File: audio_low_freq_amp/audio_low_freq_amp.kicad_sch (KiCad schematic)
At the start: 11 parts, among them Q1 NPN, Q2 PNP

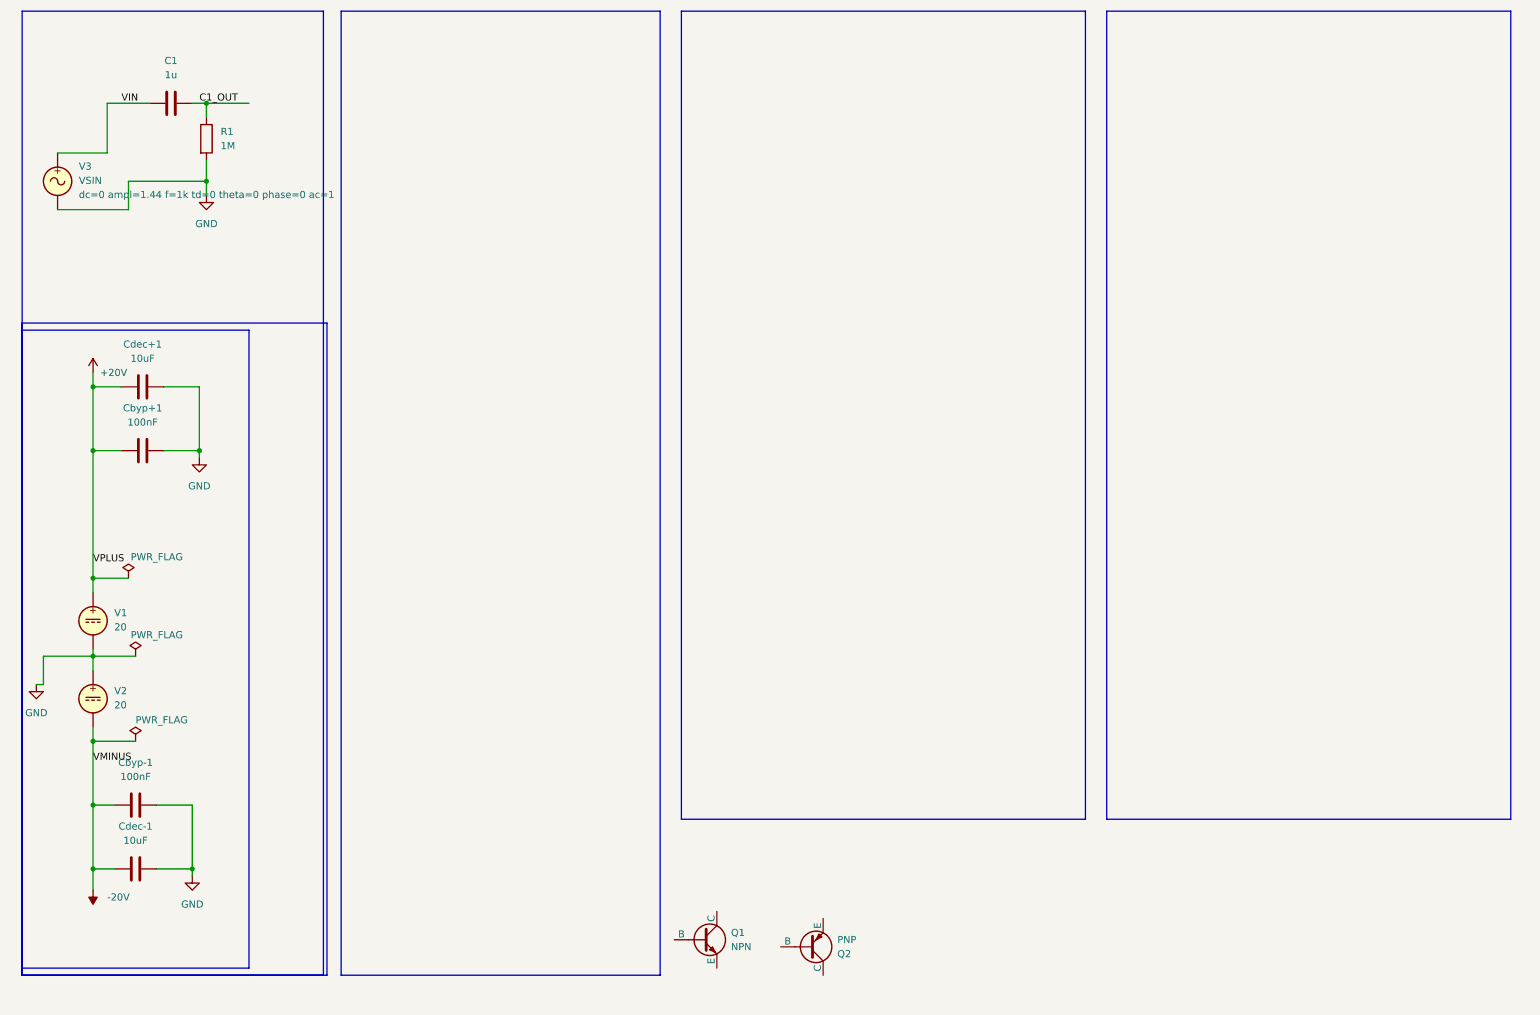
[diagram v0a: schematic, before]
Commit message: finished unrefined version of the schematic with a new approach in mind. works very good for beginning, but needs more work. great place to start bc we almost got a sine wave at output and gain is a little to big, but in normal range of error. note that at 20kHz it starts to distort a little bit
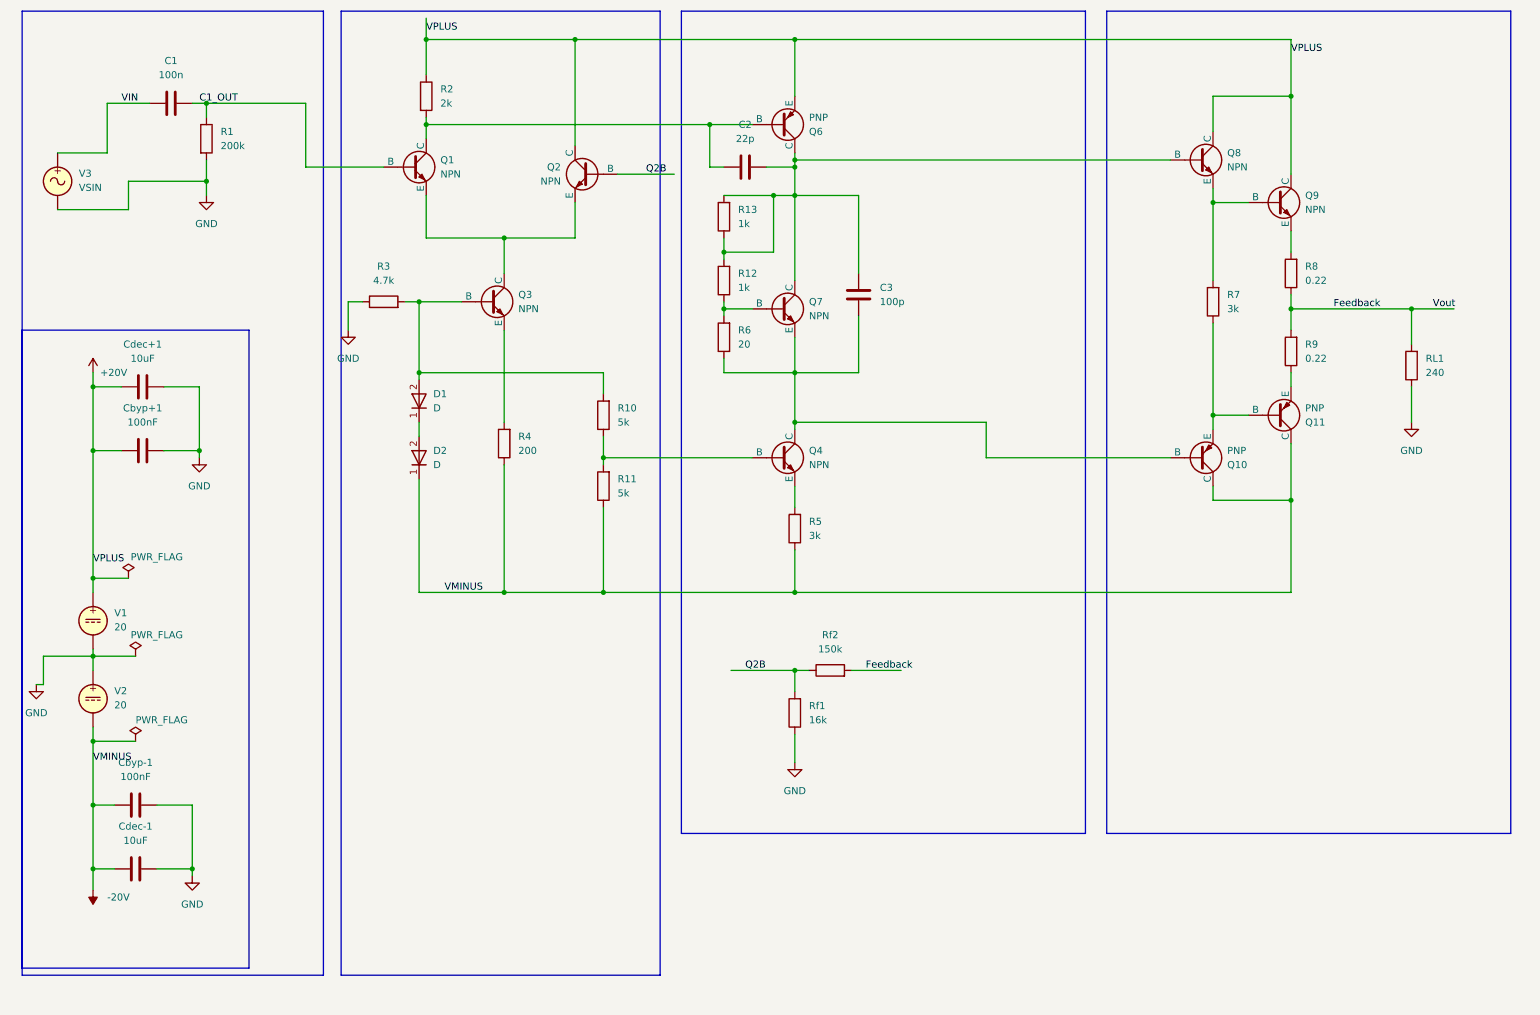
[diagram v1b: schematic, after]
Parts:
- removed Q2: PNP, symbol Simulation_SPICE:PNP
- added C2: 22p, symbol Device:C
- added C3: 100p, symbol Device:C
- added D1, D2: D, symbol Simulation_SPICE:D
- added Q10, Q11, Q6: PNP, symbol Simulation_SPICE:PNP
- added Q2, Q3, Q4, Q7, Q8, Q9: NPN, symbol Simulation_SPICE:NPN
- added R10, R11: 5k, symbol Device:R
- added R12, R13: 1k, symbol Device:R
- added R2: 2k, symbol Device:R
- added R3: 4.7k, symbol Device:R
- added R4: 200, symbol Device:R
- added R5, R7: 3k, symbol Device:R
- added R6: 20, symbol Device:R
- added R8, R9: 0.22, symbol Device:R
- added RL1: 240, symbol Device:R
- added Rf1: 16k, symbol Device:R
- added Rf2: 150k, symbol Device:R
- C1: value 1u -> 100n
- R1: value 1M -> 200k
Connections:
- net +20V: now also Q2.1 (C), Q6.3 (E), Q8.1 (C), Q9.1 (C), R2.1
- net -20V: now also D2.1 (K), Q10.1 (C), Q11.1 (C), R11.1, R4.1, R5.1
- net C1_OUT: now also Q1.2 (B)
- net GND: now also R3.1, RL1.1, Rf1.1
- net at Q1.1 (C): now also C2.1, Q6.2 (B), R2.2
- net at Q1.3 (E): now also Q2.3 (E), Q3.1 (C)
- new net: C3.1, Q10.2 (B), Q4.1 (C), Q7.3 (E), R6.1
- new net: C2.2, C3.2, Q6.1 (C), Q7.1 (C), Q8.2 (B), R12.2, R13.1, R13.2
- new net: Q4.3 (E), R5.2
- new net: Q3.3 (E), R4.2
- new net: Q10.3 (E), Q11.2 (B), R7.1
- new net: Q11.3 (E), R9.1
- new net: Q8.3 (E), Q9.2 (B), R7.2
- new net: D1.2 (A), Q3.2 (B), R10.2, R3.2
- new net: Q4.2 (B), R10.1, R11.2
- new net: D1.1 (K), D2.2 (A)
- new net: Q7.2 (B), R12.1, R6.2
- new net: Q9.3 (E), R8.2
- new net Feedback: R8.1, R9.2, RL1.2, Rf2.2
- new net Q2B: Q2.2 (B), Rf1.2, Rf2.1
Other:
- moved on the sheet: Q1

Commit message: commit before going to check up with the professor
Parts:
- removed R13: 1k, symbol Device:R
- C1: value 100n -> 100u
- C3: value 100p -> 100u
- R10: value 5k -> 3k
- R11: value 5k -> 6k
- R12: value 1k -> 2k
- R6: value 20 -> 1k
- R7: value 3k -> 5k
- Rf1: value 16k -> 10k
- Rf2: value 150k -> 90k
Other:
- moved on the sheet: R12
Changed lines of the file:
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@@
 	)
 	(junction
-		(at 148.59 52.07)
-		(diameter 0)
-		(color 0 0 0 0)
-	)
-	(junction
-		(at 139.7 62.23)
-		(diameter 0)
-		(color 0 0 0 0)
-	)
-	(junction
 		(at 152.4 123.19)
 		(diameter 0)
@@
 	(wire
 		(pts
-			(xy 139.7 71.12) (xy 139.7 72.39)
+			(xy 139.7 66.04) (xy 139.7 72.39)
 		)
 		(stroke
@@
 	(wire
 		(pts
-			(xy 139.7 62.23) (xy 139.7 59.69)
+			(xy 139.7 52.07) (xy 139.7 58.42)
 		)
 		(stroke
@@
 	(wire
 		(pts
-			(xy 139.7 62.23) (xy 148.59 62.23)
-		)
-		(stroke
-			(width 0)
-			(type default)
-		)
-	)
-	(wire
-		(pts
 			(xy 139.7 73.66) (xy 139.7 72.39)
 		)
@@
 	(wire
 		(pts
-			(xy 148.59 52.07) (xy 152.4 52.07)
-		)
-		(stroke
-			(width 0)
-			(type default)
-		)
-	)
-	(wire
-		(pts
 			(xy 262.89 72.39) (xy 262.89 78.74)
 		)
@@
 	(wire
 		(pts
-			(xy 148.59 52.07) (xy 148.59 62.23)
-		)
-		(stroke
-			(width 0)
-			(type default)
-		)
-	)
-	(wire
-		(pts
 			(xy 17.78 134.62) (xy 26.67 134.62)
 		)
@@
 	(wire
 		(pts
-			(xy 139.7 52.07) (xy 148.59 52.07)
+			(xy 139.7 52.07) (xy 152.4 52.07)
 		)
 		(stroke
@@
 	(wire
 		(pts
-			(xy 139.7 62.23) (xy 139.7 63.5)
-		)
-		(stroke
-			(width 0)
-			(type default)
-		)
-	)
-	(wire
-		(pts
 			(xy 26.67 133.35) (xy 26.67 134.62)
 		)
@@
 			)
 		)
-		(property "Value" "100n"
+		(property "Value" "100u"
 			(at 40.64 30.48 90)
 			(effects
@@
 			)
 		)
-		(property "Value" "100p"
+		(property "Value" "100u"
 			(at 167.64 71.1199 0)
 			(effects
@@
 			)
 		)
-		(property "Sim.Params" "dc=0 ampl=1.44 f=20k td=0 theta=0 phase=0 ac=1"
+		(property "Sim.Params" "dc=0 ampl=1.44 f=10k td=0 theta=0 phase=0 ac=1"
 			(at 24.13 51.9401 0)
 			(effects
@@
 	)
 	(symbol
-		(lib_id "Device:R")
-		(at 139.7 55.88 180)
-		(unit 1)
-		(exclude_from_sim no)
-		(in_bom yes)
-		(on_board yes)
-		(dnp no)
-		(fields_autoplaced yes)
-		(property "Reference" "R13"
-			(at 142.24 54.6099 0)
-			(effects
-				(font
-					(size 1.27 1.27)
-				)
-				(justify right)
-			)
-		)
-		(property "Value" "1k"
-			(at 142.24 57.1499 0)
-			(effects
-				(font
-					(size 1.27 1.27)
-				)
-				(justify right)
-			)
-		)
-		(property "Footprint" ""
-			(at 141.478 55.88 90)
-			(effects
-				(font
-					(size 1.27 1.27)
-				)
-				(hide yes)
-			)
-		)
-		(property "Datasheet" "~"
-			(at 139.7 55.88 0)
-			(effects
-				(font
-					(size 1.27 1.27)
-				)
-				(hide yes)
-			)
-		)
-		(property "Description" "Resistor"
-			(at 139.7 55.88 0)
-			(effects
-				(font
-					(size 1.27 1.27)
-				)
-				(hide yes)
-			)
-		)
-		(pin "2"
-		)
-		(pin "1"
-		)
-		(instances
-			(project "audio_low_freq_amp"
-				(path "/81945fdf-1028-429c-9d81-15fb539a69d7"
-					(reference "R13")
-					(unit 1)
-				)
-			)
-		)
-	)
-	(symbol
 		(lib_id "Simulation_SPICE:PNP")
 		(at 238.76 91.44 0)
@@
 			)
 		)
-		(property "Value" "5k"
+		(property "Value" "3k"
 			(at 120.65 92.7099 0)
 			(effects
@@
 	(symbol
 		(lib_id "Device:R")
-		(at 139.7 67.31 180)
+		(at 139.7 62.23 180)
 		(unit 1)
 		(exclude_from_sim no)
@@
 		(fields_autoplaced yes)
 		(property "Reference" "R12"
-			(at 142.24 66.0399 0)
+			(at 142.24 60.9599 0)
 			(effects
 				(font
@@
 			)
 		)
-		(property "Value" "1k"
-			(at 142.24 68.5799 0)
+		(property "Value" "2k"
+			(at 142.24 63.4999 0)
 			(effects
 				(font
@@
 		)
 		(property "Footprint" ""
-			(at 141.478 67.31 90)
+			(at 141.478 62.23 90)
 			(effects
 				(font
@@
 		)
 		(property "Datasheet" "~"
-			(at 139.7 67.31 0)
+			(at 139.7 62.23 0)
 			(effects
 				(font
@@
 		)
 		(property "Description" "Resistor"
-			(at 139.7 67.31 0)
+			(at 139.7 62.23 0)
 			(effects
 				(font
@@
 			)
 		)
-		(property "Value" "5k"
+		(property "Value" "6k"
 			(at 120.65 105.4099 0)
 			(effects
@@
 			)
 		)
-		(property "Value" "16k"
+		(property "Value" "10k"
 			(at 154.94 146.0499 0)
 			(effects
@@
 			)
 		)
-		(property "Value" "3k"
+		(property "Value" "5k"
 			(at 229.87 72.3899 0)
 			(effects
@@
 			)
 		)
-		(property "Value" "20"
+		(property "Value" "1k"
 			(at 142.24 78.7399 0)
 			(effects
@@
 			)
 		)
-		(property "Value" "150k"
+		(property "Value" "90k"
 			(at 158.75 133.35 90)
 			(effects

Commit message: modified final sch in tina and kicad
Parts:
- removed Q1, Q2: NPN, symbol Simulation_SPICE:NPN
- removed Q10, Q6: PNP, symbol Simulation_SPICE:PNP
- removed R11: 6k, symbol Device:R
- removed Rf1: 10k, symbol Device:R
- removed Rf2: 90k, symbol Device:R
- added C4: 10u, symbol Device:C
- added D3, D4: LED, LED_SMD:LED_0805_2012Metric, symbol Device:LED
- added Q1, Q11, Q2, Q5, Q8: PNP, symbol Simulation_SPICE:PNP
- added Q12, Q6: NPN, symbol Simulation_SPICE:NPN
- added R13: 2.7k, Resistor_SMD:R_0805_2012Metric, symbol Device:R
- added R14: 100, Resistor_SMD:R_0805_2012Metric, symbol Device:R
- added R15, R18: 2, Resistor_SMD:R_0805_2012Metric, symbol Device:R
- added R19: 1, Resistor_SMD:R_0805_2012Metric, symbol Device:R
- added R20, R21: 2.2k, Resistor_SMD:R_0805_2012Metric, symbol Device:R
- added R7: 15k, Resistor_SMD:R_0805_2012Metric, symbol Device:R
- added R8: 9.1k, Resistor_SMD:R_0805_2012Metric, symbol Device:R
- added R9: 1.8k, Resistor_SMD:R_0805_2012Metric, symbol Device:R
- added RL2, RL3: 10, symbol Device:R
- added RV1: 1k, Potentiometer_SMD:Potentiometer_Vishay_TS53YL_Vertical, symbol Device:R_Potentiometer
- C1, C3: value 100u -> 10u
- C2: value 22p -> 10u
- R1: value 200k -> 100k; footprint (none) -> Resistor_SMD:R_0805_2012Metric
- R10: value 3k -> 100k; footprint (none) -> Resistor_SMD:R_0805_2012Metric
- R11: renamed from R7; value 5k -> 470; footprint (none) -> Resistor_SMD:R_0805_2012Metric
- R12: value 2k -> 2.2k; footprint (none) -> Resistor_SMD:R_0805_2012Metric
- R16: renamed from R8; value 0.22 -> 2; footprint (none) -> Resistor_SMD:R_0805_2012Metric
- R17: renamed from R9; value 0.22 -> 2; footprint (none) -> Resistor_SMD:R_0805_2012Metric
- R2: value 2k -> 100; footprint (none) -> Resistor_SMD:R_0805_2012Metric
- R3: value 4.7k -> 100; footprint (none) -> Resistor_SMD:R_0805_2012Metric
- R4: value 200 -> 470; footprint (none) -> Resistor_SMD:R_0805_2012Metric
- R5: value 3k -> 100; footprint (none) -> Resistor_SMD:R_0805_2012Metric
- R6: value 1k -> 100; footprint (none) -> Resistor_SMD:R_0805_2012Metric
- RL1: value 240 -> 220
- renumbered Q8 to Q10, Q11 to Q13
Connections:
- net +20V: now also D1.2 (A), R4.1, D3.1 (K), Q12.1 (C), R14.1, R21.1; no longer Q9.1 (C), R2.1
- net -20V: now also Q7.3 (E), R12.2, R5.2, R6.2, D4.1 (K), Q11.1 (C); no longer D2.1 (K), R4.1, R5.1
- net Feedback: now also R10.1, Q2.2 (B), R8.1; no longer R16.1, R17.2, RL1.2
- net GND: now also C2.1, Q6.1 (C), R20.1, R7.2, RL3.1; no longer R3.1, RL1.1
- net at C3.1, Q4.1 (C): now also Q1.1 (C), Q6.2 (B); no longer Q7.3 (E), R6.1
- net at Q4.3 (E): now also R5.1; no longer R5.2
- net at Q3.1 (C): now also Q3.2 (B), Q4.2 (B), Q2.1 (C)
- net at R4.2: now also Q5.3 (E); no longer Q3.3 (E)
- net at Q13.2 (B), R11.1: now also Q11.3 (E)
- net at Q13.3 (E): now also R18.1; no longer R17.1
- net at Q10.3 (E), R11.2: now also Q12.2 (B); no longer Q9.2 (B)
- net at Q7.2 (B), R12.1: now also Q6.3 (E); no longer R6.2
- net at R2.2: now also Q1.3 (E); no longer C2.1
- net at Q9.3 (E): now also C3.2, Q7.1 (C), C4.1, Q11.2 (B), RV1.2, RV1.3; no longer R16.2
- net C1_OUT: no longer names the net of C1.2, R1.1
- net C1_OUT: now also Q1.2 (B)
- new net: C2.2, R9.2
- new net: C4.2, Q10.2 (B), Q8.1 (C), Q9.1 (C), R13.1
- new net: Q9.2 (B), R13.2, RV1.1
- new net: Q5.1 (C), R2.1, R3.1
- new net: D2.1 (K), Q5.2 (B), Q8.2 (B), R7.1
- new net: Q3.3 (E), R6.1
- new net: Q2.3 (E), R3.2
- new net: D4.2 (A), R20.2
- new net: RL2.1, RL3.2
- new net: R16.1, R17.2, R19.2
- new net: Q8.3 (E), R14.2
- new net: R15.1, R16.2
- new net: Q12.3 (E), R15.2
- new net: D3.2 (A), R21.2
- new net: R8.2, R9.1
- new net: RL1.1, RL2.2
- new net: R17.1, R18.2
- new net Vout: R10.2, R19.1, RL1.2
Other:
- moved on the sheet: Q10, Q13, R1, R11, R16, R17, RL1, V2, V3
